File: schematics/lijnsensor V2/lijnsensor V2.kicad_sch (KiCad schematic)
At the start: 31 parts, among them J1 Conn_01x04_Pin, U1 USBLC6-2SC6, U10 AS7343xDLG, U11 AS7343xDLG, U2 TCA9548APWR, U3 TLV75718PDBV, U4 AS7343xDLG, U5 AS7343xDLG, U6 AS7343xDLG, U7 AS7343xDLG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

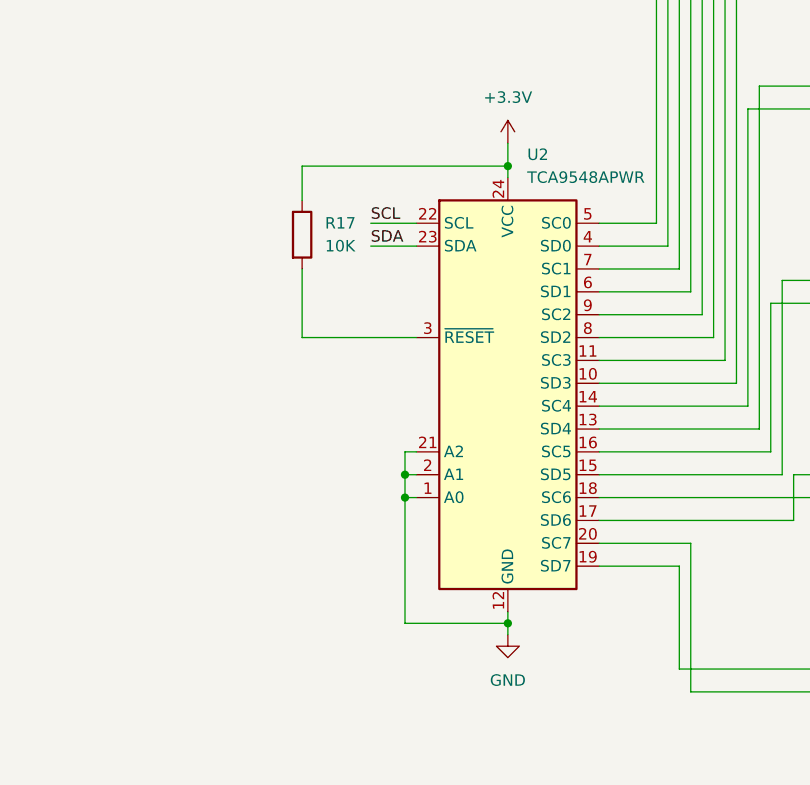
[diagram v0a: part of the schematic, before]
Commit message: verander het I²C adders van de I²C multiplexer om conflict te vermijden
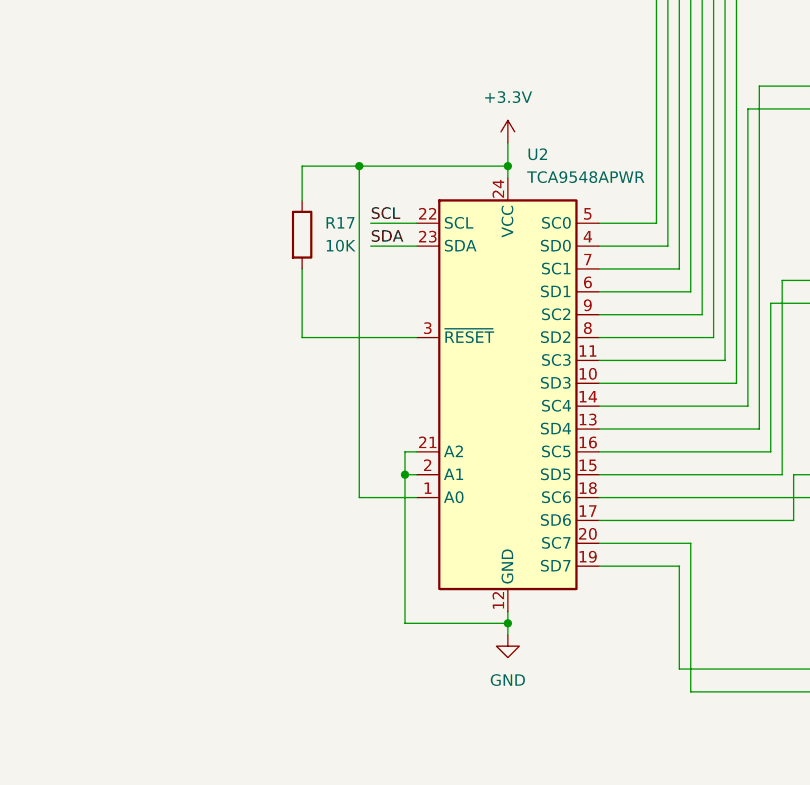
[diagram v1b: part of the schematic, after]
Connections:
- net +3.3V: now also U2.1 (A0)
- net GND: no longer U2.1 (A0)
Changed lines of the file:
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@@
+	)
+	(junction
+		(at 73.66 125.73)
+		(diameter 0)
+		(color 255 0 0 1)
 	)
 	(junction
@@
 	)
 	(junction
-		(at 78.74 162.56)
+		(at 72.39 38.1)
 		(diameter 0)
 		(color 0 0 0 1)
 	)
 	(junction
-		(at 72.39 38.1)
+		(at 147.32 64.77)
+		(diameter 0)
+		(color 255 0 0 1)
+	)
+	(junction
+		(at 125.73 29.21)
+		(diameter 0)
+		(color 0 0 0 0)
+	)
+	(junction
+		(at 165.1 105.41)
 		(diameter 0)
 		(color 0 0 0 1)
 	)
 	(junction
-		(at 147.32 64.77)
-		(diameter 0)
-		(color 255 0 0 1)
-	)
-	(junction
-		(at 125.73 29.21)
+		(at 165.1 60.96)
+		(diameter 0)
+		(color 0 0 0 1)
+	)
+	(junction
+		(at 133.35 162.56)
 		(diameter 0)
 		(color 0 0 0 0)
 	)
 	(junction
-		(at 165.1 105.41)
+		(at 147.32 20.32)
+		(diameter 0)
+		(color 255 0 0 1)
+	)
+	(junction
+		(at 90.17 176.53)
+		(diameter 0)
+		(color 0 0 0 0)
+	)
+	(junction
+		(at 149.86 60.96)
 		(diameter 0)
 		(color 0 0 0 1)
 	)
 	(junction
-		(at 165.1 60.96)
+		(at 133.35 184.15)
+		(diameter 0)
+		(color 0 0 0 0)
+	)
+	(junction
+		(at 133.35 97.79)
+		(diameter 0)
+		(color 0 0 0 0)
+	)
+	(junction
+		(at 165.1 148.59)
 		(diameter 0)
 		(color 0 0 0 1)
 	)
 	(junction
-		(at 133.35 162.56)
+		(at 125.73 116.84)
 		(diameter 0)
 		(color 0 0 0 0)
 	)
 	(junction
-		(at 147.32 20.32)
-		(diameter 0)
-		(color 255 0 0 1)
-	)
-	(junction
-		(at 90.17 176.53)
+		(at 147.32 129.54)
+		(diameter 0)
+		(color 255 0 0 1)
+	)
+	(junction
+		(at 133.35 41.91)
+		(diameter 0)
+		(color 255 0 0 1)
+	)
+	(junction
+		(at 133.35 86.36)
+		(diameter 0)
+		(color 255 0 0 1)
+	)
+	(junction
+		(at 133.35 107.95)
+		(diameter 0)
+		(color 255 0 0 1)
+	)
+	(junction
+		(at 133.35 76.2)
 		(diameter 0)
 		(color 0 0 0 0)
 	)
-	(junction
-		(at 149.86 60.96)
-		(diameter 0)
-		(color 0 0 0 1)
-	)
-	(junction
-		(at 133.35 184.15)
-		(diameter 0)
-		(color 0 0 0 0)
-	)
-	(junction
-		(at 133.35 97.79)
-		(diameter 0)
-		(color 0 0 0 0)
-	)
-	(junction
-		(at 165.1 148.59)
-		(diameter 0)
-		(color 0 0 0 1)
-	)
-	(junction
-		(at 125.73 116.84)
-		(diameter 0)
-		(color 0 0 0 0)
-	)
-	(junction
-		(at 147.32 129.54)
-		(diameter 0)
-		(color 255 0 0 1)
-	)
-	(junction
-		(at 133.35 41.91)
-		(diameter 0)
-		(color 255 0 0 1)
-	)
-	(junction
-		(at 133.35 86.36)
-		(diameter 0)
-		(color 255 0 0 1)
-	)
-	(junction
-		(at 133.35 107.95)
-		(diameter 0)
-		(color 255 0 0 1)
-	)
-	(junction
-		(at 133.35 76.2)
-		(diameter 0)
-		(color 0 0 0 0)
-	)
 	(no_connect
 		(at 137.16 143.51)
@@
 	(wire
 		(pts
-			(xy 90.17 125.73) (xy 67.31 125.73)
+			(xy 90.17 125.73) (xy 73.66 125.73)
 		)
 		(stroke
@@
 	(wire
 		(pts
+			(xy 73.66 162.56) (xy 80.01 162.56)
+		)
+		(stroke
+			(width 0)
+			(type default)
+			(color 255 0 0 1)
+		)
+	)
+	(wire
+		(pts
 			(xy 133.35 27.94) (xy 133.35 31.75)
 		)
@@
 	(wire
 		(pts
+			(xy 73.66 125.73) (xy 73.66 162.56)
+		)
+		(stroke
+			(width 0)
+			(type default)
+			(color 255 0 0 1)
+		)
+	)
+	(wire
+		(pts
 			(xy 147.32 172.72) (xy 167.64 172.72)
 		)
@@
 	(wire
 		(pts
-			(xy 78.74 162.56) (xy 78.74 160.02)
-		)
-		(stroke
-			(width 0)
-			(type default)
-			(color 0 0 0 1)
-		)
-	)
-	(wire
-		(pts
 			(xy 125.73 138.43) (xy 120.65 138.43)
 		)
@@
 	(wire
 		(pts
-			(xy 78.74 176.53) (xy 78.74 162.56)
+			(xy 78.74 160.02) (xy 78.74 176.53)
 		)
 		(stroke
@@
 	(wire
 		(pts
+			(xy 73.66 125.73) (xy 67.31 125.73)
+		)
+		(stroke
+			(width 0)
+			(type default)
+			(color 255 0 0 1)
+		)
+	)
+	(wire
+		(pts
 			(xy 78.74 160.02) (xy 80.01 160.02)
 		)
@@
 		)
 		(stroke
-			(width 0)
-			(type default)
-			(color 0 0 0 1)
-		)
-	)
-	(wire
-		(pts
-			(xy 78.74 162.56) (xy 80.01 162.56)
-		)
-		(stroke

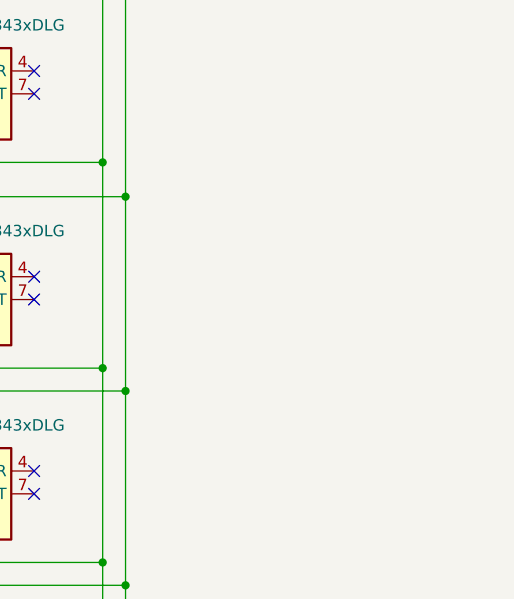
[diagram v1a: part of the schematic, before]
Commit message: pas de maten aan van de addon V3 en de lijnsensor(nog niet klaar)
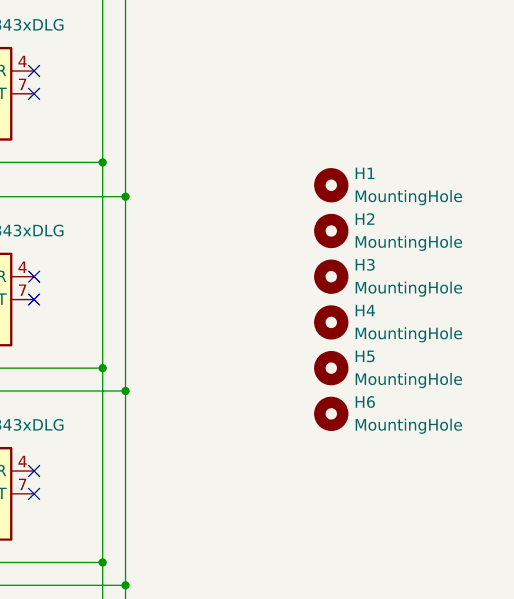
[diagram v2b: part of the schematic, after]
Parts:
- added H1, H2, H3, H4: MountingHole, MountingHole:MountingHole_4.3mm_M4, symbol Mechanical:MountingHole
- added H5, H6: MountingHole, MountingHole:MountingHole_8.4mm_M8, symbol Mechanical:MountingHole
